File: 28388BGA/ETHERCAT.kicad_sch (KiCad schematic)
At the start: 37 parts, among them Q13 DP83822IRHBR

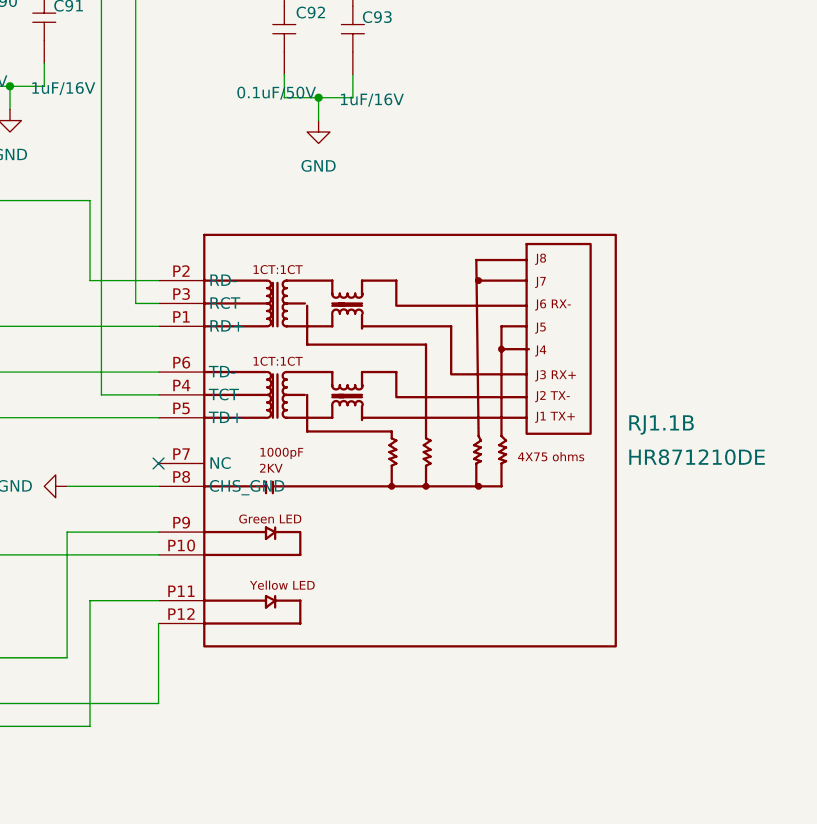
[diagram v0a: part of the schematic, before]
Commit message: 增加16Pins ADC接口，修改EtherCAT接口顺序，修改ADR423输入电源电压为5V
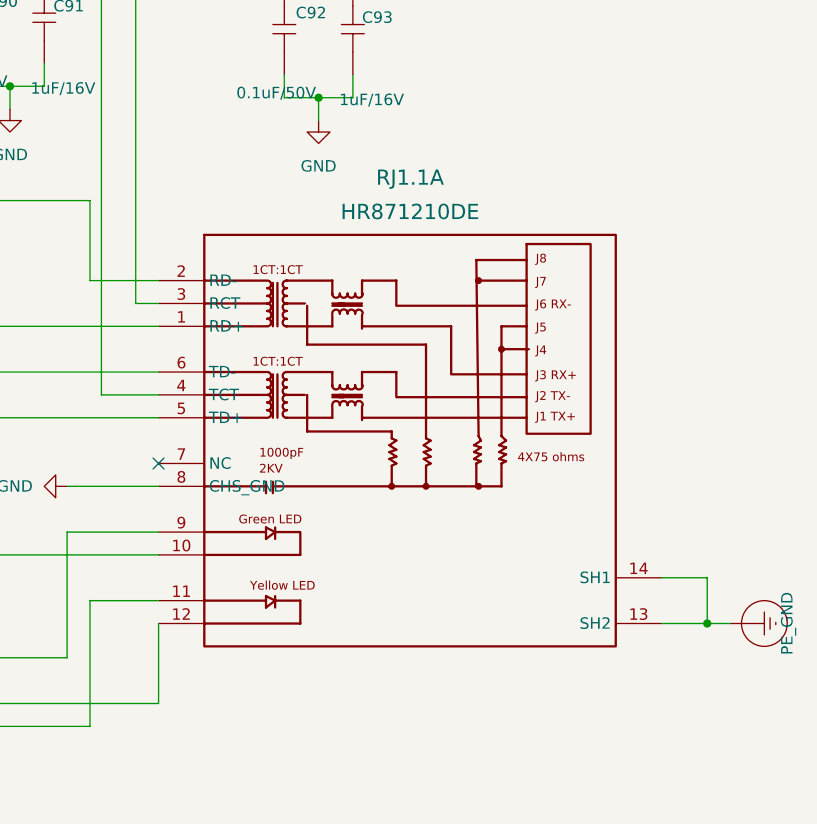
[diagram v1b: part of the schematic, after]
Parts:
- removed RJ1.1: HR871210DE, Lib4:RJ45-TH_HR871210DE, symbol sheet1-altium-import:HR871210DE
- added RJ1.1: HR871210DE, Lib4:RJ45-TH_HR871210DE, symbol sheet1-altium-import:HR871210DE
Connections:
- net +3V3D_DSP: now also RJ1.1.3 (RCT), RJ1.1.4 (TCT)
- net ESC_LED_LINK: now also RJ1.1.10
- net ESC_PHY: now also RJ1.1.12
- net GND: now also RJ1.1.8 (CHS_GND)
- net at Q13.10 (RD_P), R84.1: now also RJ1.1.1 (RD+)
- net at R87.2: now also RJ1.1.11
- net at Q13.9 (RD_M), R85.1: now also RJ1.1.2 (RD-)
- net at Q13.12 (TD_P), R81.1: now also RJ1.1.5 (TD+)
- net at Q13.11 (TD_M), R82.1: now also RJ1.1.6 (TD-)
- net at R86.2: now also RJ1.1.9
- new net PE_GND: RJ1.1.13 (SH2), RJ1.1.14 (SH1)
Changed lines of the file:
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@@
 	)
 	(junction
+		(at 290.83 125.73)
+		(diameter 0)
+		(color 0 0 0 0)
+	)
+	(junction
 		(at 177.8 99.06)
 		(diameter 0)
@@
 	(wire
 		(pts
+			(xy 285.75 120.65) (xy 290.83 120.65)
+		)
+		(stroke
+			(width 0)
+			(type default)
+		)
+	)
+	(wire
+		(pts
 			(xy 154.94 97.79) (xy 154.94 101.6)
 		)
@@
 	(wire
 		(pts
+			(xy 285.75 125.73) (xy 290.83 125.73)
+		)
+		(stroke
+			(width 0)
+			(type default)
+		)
+	)
+	(wire
+		(pts
 			(xy 22.86 38.1) (xy 22.86 35.56)
 		)
@@
 	(wire
 		(pts
+			(xy 290.83 120.65) (xy 290.83 125.73)
+		)
+		(stroke
+			(width 0)
+			(type default)
+		)
+	)
+	(wire
+		(pts
 			(xy 170.18 40.64) (xy 180.34 40.64)
 		)
@@
 	(wire
 		(pts
+			(xy 293.37 125.73) (xy 290.83 125.73)
+		)
+		(stroke
+			(width 0)
+			(type default)
+		)
+	)
+	(wire
+		(pts
 			(xy 222.25 78.74) (xy 222.25 87.63)
 		)
@@
 	)
 	(symbol
-		(lib_id "sheet1-altium-import:HR871210DE")
-		(at 257.81 105.41 0)
-		(unit 2)
+		(lib_id "power:Earth_Protective")
+		(at 293.37 125.73 90)
+		(unit 1)
 		(exclude_from_sim no)
 		(in_bom yes)
 		(on_board yes)
 		(dnp no)
-		(fields_autoplaced yes)
-		(property "Reference" "RJ1.1"
-			(at 281.94 103.5049 0)
-			(effects
-				(font
-					(face "Arial")
-					(size 1.6891 1.6891)
-				)
-				(justify left)
-			)
-		)
-		(property "Value" "HR871210DE"
-			(at 281.94 107.3149 0)
-			(effects
-				(font
-					(face "Arial")
-					(size 1.6891 1.6891)
-				)
-				(justify left)
-			)
-		)
-		(property "Footprint" "Lib4:RJ45-TH_HR871210DE"
-			(at 257.81 105.41 0)
-			(effects
-				(font
-					(size 1.27 1.27)
-				)
-				(hide yes)
-			)
-		)
-		(property "Datasheet" ""
-			(at 257.81 105.41 0)
-			(effects
-				(font
-					(size 1.27 1.27)
-				)
-				(hide yes)
-			)
-		)
-		(property "Description" ""
-			(at 257.81 105.41 0)
+		(property "Reference" "#PWR0263"
+			(at 293.37 125.73 0)
 			(effects
 				(font
@@
 			)
 		)
-		(property "Manufacturer Part" "HR871210DE"
-			(at 257.81 105.41 0)
+		(property "Value" "PE_GND"
+			(at 299.72 125.73 0)
 			(effects
 				(font
 					(size 1.27 1.27)
 				)
-				(hide yes)
 			)
 		)
-		(property "Manufacturer" "HANRUN(汉仁)"
-			(at 257.81 105.41 0)
+		(property "Footprint" ""
+			(at 295.91 125.73 0)
 			(effects
 				(font
@@
 			)
 		)
-		(property "Supplier Part" "C19724758"
-			(at 257.81 105.41 0)
+		(property "Datasheet" "~"
+			(at 295.91 125.73 0)
 			(effects
 				(font
@@
 			)
 		)
-		(property "Supplier" "LCSC"
-			(at 257.81 105.41 0)
+		(property "Description" "Power symbol creates a global label with name \"Earth_Protective\""
+			(at 293.37 125.73 0)
 			(effects
 				(font
@@
 			)
 		)
-		(pin "7"
-		)
-		(pin "4"
-		)
-		(pin "5"
-		)
 		(pin "1"
 		)
-		(pin "9"
-		)
-		(pin "10"
-		)
-		(pin "12"
-		)
-		(pin "6"
-		)
-		(pin "3"
-		)
-		(pin "11"
-		)
-		(pin "2"
-		)
-		(pin "8"
-		)
-		(pin "13"
-		)
-		(pin "14"
-		)
-		(pin "P2"
-		)
-		(pin "P6"
-		)
-		(pin "P1"
-		)
-		(pin "P4"
-		)
-		(pin "P7"
-		)
-		(pin "P8"
-		)
-		(pin "P9"
-		)
-		(pin "P3"
-		)
-		(pin "P5"
-		)
-		(pin "P12"
-		)
-		(pin "P11"
-		)
-		(pin "P10"
-		)
 		(instances
 			(project "28388bga"
 				(path "/88c87a56-bf0e-49aa-812f-d0846700c8ff/bf400ea6-5cda-4f86-b4fb-e22cb5ac67d9"
-					(reference "RJ1.1")
-					(unit 2)
+					(reference "#PWR0263")
+					(unit 1)
 				)
 			)
@@
 					(unit 1)
 				)
+			)
+		)
+	)
+	(symbol
+		(lib_id "sheet1-altium-import:HR871210DE")
+		(at 257.81 105.41 0)
+		(unit 1)
+		(exclude_from_sim no)
+		(in_bom yes)
+		(on_board yes)
+		(dnp no)
+		(fields_autoplaced yes)
+		(property "Reference" "RJ1.1"
+			(at 257.81 76.2 0)
+			(effects
+				(font
+					(face "Arial")
+					(size 1.6891 1.6891)
+				)
+			)
+		)
+		(property "Value" "HR871210DE"
+			(at 257.81 80.01 0)
+			(effects
+				(font
+					(face "Arial")
+					(size 1.6891 1.6891)
+				)
+			)
+		)
+		(property "Footprint" "Lib4:RJ45-TH_HR871210DE"
+			(at 257.81 105.41 0)
+			(effects
+				(font
+					(size 1.27 1.27)
+				)
+				(hide yes)
+			)
+		)
+		(property "Datasheet" ""
+			(at 257.81 105.41 0)
+			(effects
+				(font
+					(size 1.27 1.27)
+				)
+				(hide yes)
+			)
+		)
+		(property "Description" ""
+			(at 257.81 105.41 0)
+			(effects
+				(font
+					(size 1.27 1.27)
+				)
+				(hide yes)
+			)
+		)
+		(property "Manufacturer Part" "HR871210DE"
+			(at 257.81 105.41 0)
+			(effects
+				(font
+					(size 1.27 1.27)
+				)
+				(hide yes)
+			)
+		)
+		(property "Manufacturer" "HANRUN(汉仁)"
+			(at 257.81 105.41 0)
+			(effects
+				(font
+					(size 1.27 1.27)
+				)
+				(hide yes)
+			)
+		)
+		(property "Supplier Part" "C19724758"
+			(at 257.81 105.41 0)
+			(effects
+				(font
+					(size 1.27 1.27)
+				)
+				(hide yes)
+			)
+		)
+		(property "Supplier" "LCSC"
+			(at 257.81 105.41 0)
+			(effects
+				(font
+					(size 1.27 1.27)
+				)
+				(hide yes)
+			)
+		)
+		(pin "7"
+		)
+		(pin "4"
+		)
+		(pin "5"
+		)
+		(pin "1"
+		)
+		(pin "9"
+		)
+		(pin "10"
+		)
+		(pin "12"
+		)
+		(pin "6"
+		)
+		(pin "3"
+		)
+		(pin "11"
+		)
+		(pin "2"
+		)
+		(pin "8"
+		)
+		(pin "13"
+		)
+		(pin "14"
+		)
+		(pin "P2"
+		)
+		(pin "P6"
+		)
+		(pin "P1"
+		)
+		(pin "P4"
+		)
+		(pin "P7"
+		)
+		(pin "P8"
+		)
+		(pin "P9"
+		)
+		(pin "P3"
+		)
+		(pin "P5"
+		)
+		(pin "P12"
+		)
+		(pin "P11"
+		)
+		(pin "P10"
+		)
+		(instances
+			(project "28388bga"
+				(path "/88c87a56-bf0e-49aa-812f-d0846700c8ff/bf400ea6-5cda-4f86-b4fb-e22cb5ac67d9"
+					(reference "RJ1.1")
+					(unit 1)
+				)
